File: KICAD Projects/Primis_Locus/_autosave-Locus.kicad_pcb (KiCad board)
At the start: 4 copper layers, 40 x 40 mm, 63 parts, among them J1 Conn_ARM_SWD_TagConnect_TC203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, J2 S2B-PH-SM4-TB_LF_SN, J4 USB_C_Receptacle_USB2.0_16P, SW1 SW_DPST_x2, U1 nRF52833_QDxx, U2 LSM6DSV16XTR, U3 QMC6309, U5 MCP73831T-2ATI_OT, Y1 32.768kHz, Y2 32MHz

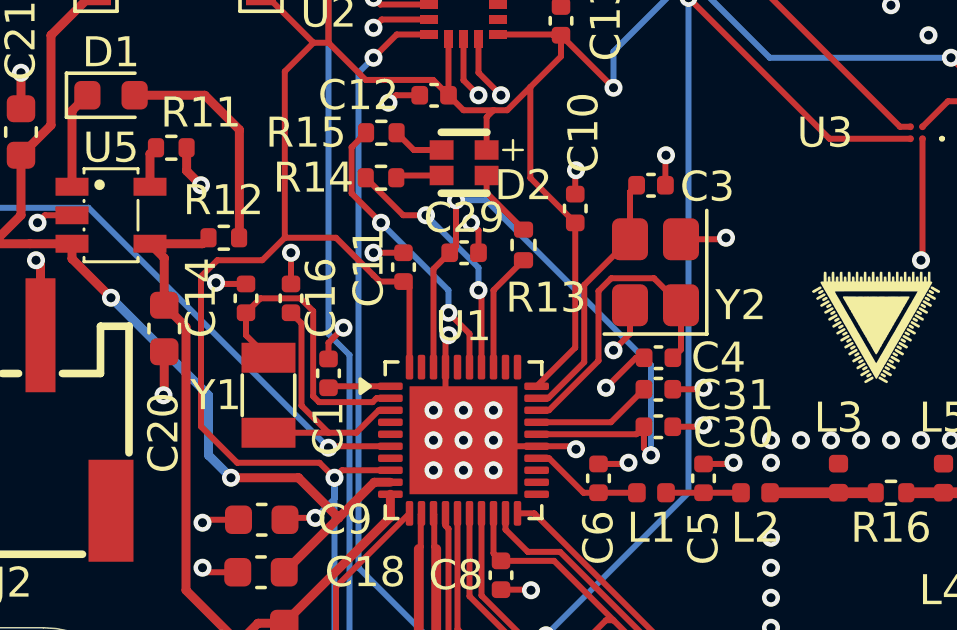
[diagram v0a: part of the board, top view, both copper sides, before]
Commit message: Locus EV1 Crystal Fix
-One last crystal fixed, there good for real this time ordered
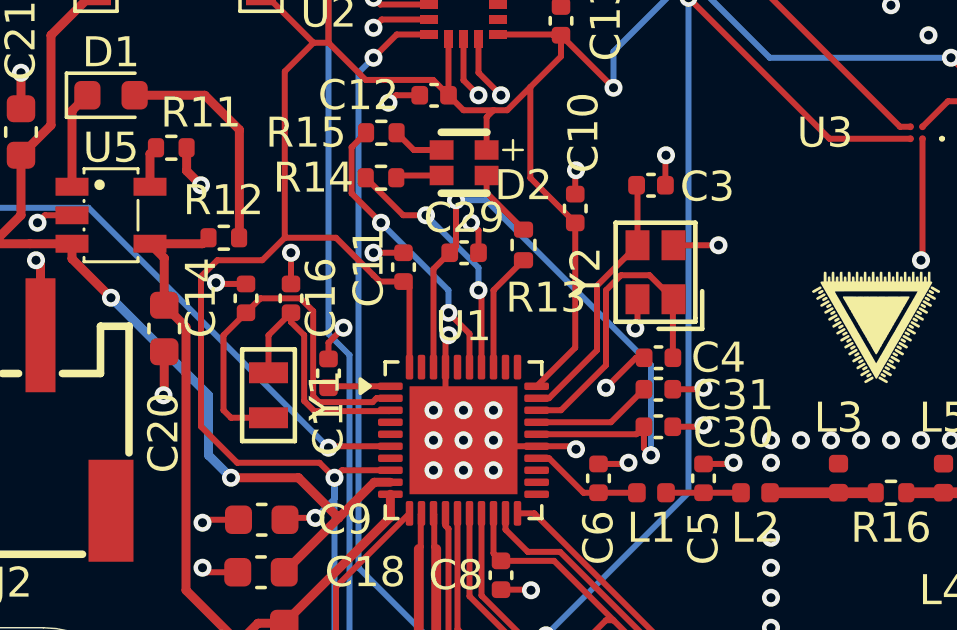
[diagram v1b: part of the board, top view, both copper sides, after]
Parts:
- Y1: footprint Crystal:Crystal_SMD_3215-2Pin_3.2x1.5mm -> primis2:SC-20S32_768kHz20PPM9pF
- Y2: footprint Crystal:Crystal_SMD_Abracon_ABM8G-4Pin_3.2x2.5mm -> primis2:NX2016SA-32MHZ-STD-CZS-5
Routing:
- net Net-(U1-XL1/P0.00): track 9.97 -> 13.3 mm
- net GND: track 71.6 -> 70.8 mm
